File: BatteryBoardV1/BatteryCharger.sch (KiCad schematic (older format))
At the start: 11 parts, among them J1 Conn_01x04_Male, Q1 Q_NMOS_GSD, U1 MCP73213

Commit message: Rearrange components to add mounting holes and silkscreen
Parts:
- added MK1, MK2, MK3: Mounting_Hole, Mounting_Holes:MountingHole_3.2mm_M3, symbol Mounting_Hole
- J1: renamed from JIn1; footprint Connectors:Barrel_Jack_CUI_PJ-102AH -> SOAR_Kicad_Library:CUI_PJ-102A_2.5mm_DC_JACK
- J2: renamed from JIn2; footprint TerminalBlock_Phoenix:TerminalBlock_Phoenix_PT-1,5-2-5.0-H_1x02_P5.00mm_Horizontal -> SOAR_Kicad_Library:TerminalBlock_5mm_2POS_ED2600
- J3: renamed from J1; footprint SOAR_Library:Molex_Micro-Fit_3.0_43045-0400_2x02_P3.00mm_Horizontal -> SOAR_Kicad_Library:Molex_Micro-Fit_3.0_43045-0400_2x02_P3.00mm_Horizontal
- J4: renamed from JOut1; footprint TerminalBlock_Phoenix:TerminalBlock_Phoenix_PT-1,5-2-5.0-H_1x02_P5.00mm_Horizontal -> SOAR_Kicad_Library:TerminalBlock_5mm_2POS_ED2600
- renumbered C2 to C1, C1 to C2
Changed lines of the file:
@@
 LIBS:valves
 LIBS:BatCharge
-LIBS:Connectors
-LIBS:dk_Addressable-Specialty
-LIBS:dk_Alarms-Buzzers-and-Sirens
-LIBS:dk_Automotive-Relays
-LIBS:dk_Balun
-LIBS:dk_Barrel-Audio-Connectors
-LIBS:dk_Battery-Holders-Clips-Contacts
-LIBS:dk_Clock-Timing-Clock-Generators-PLLs-Frequency-Synthesizers
-LIBS:dk_Clock-Timing-Programmable-Timers-and-Oscillators
-LIBS:dk_Clock-Timing-Real-Time-Clocks
-LIBS:dk_Coaxial-Connectors-RF
-LIBS:dk_Current-Transducers
-LIBS:dk_Data-Acquisition-ADCs-DACs-Special-Purpose
-LIBS:dk_Data-Acquisition-Analog-to-Digital-Converters-ADC
-LIBS:dk_Data-Acquisition-Digital-Potentiometers
-LIBS:dk_Data-Acquisition-Digital-to-Analog-Converters-DAC
-LIBS:dk_Data-Acquisition-Touch-Screen-Controllers
-LIBS:dk_DC-DC-Converters
-LIBS:dk_Digital-Isolators
-LIBS:dk_Diodes-Bridge-Rectifiers
-LIBS:dk_Diodes-Rectifiers-Arrays
-LIBS:dk_Diodes-Rectifiers-Single
-LIBS:dk_Diodes-Zener-Single
-LIBS:dk_Display-Modules-LED-Character-and-Numeric
-LIBS:dk_D-Sub-Connectors
-LIBS:dk_Embedded-Microcontrollers
-LIBS:dk_Encoders
-LIBS:dk_Evaluation-Boards-Sensors
-LIBS:dk_Ferrite-Beads-and-Chips
-LIBS:dk_Fixed-Inductors
-LIBS:dk_Fuses
-LIBS:dk_Gas-Sensors
-LIBS:dk_Humidity-Moisture-Sensors
-LIBS:dk_Image-Sensors-Camera
-LIBS:dk_Infrared-UV-Visible-Emitters
-LIBS:dk_Inrush-Current-Limiters-ICL
-LIBS:dk_Interface-Analog-Switches-Multiplexers-Demultiplexers
-LIBS:dk_Interface-Analog-Switches-Special-Purpose
-LIBS:dk_Interface-Controllers
-LIBS:dk_Interface-Drivers-Receivers-Transceivers
-LIBS:dk_Interface-I-O-Expanders
-LIBS:dk_Interface-Modules
-LIBS:dk_Interface-Sensor-and-Detector-Interfaces
-LIBS:dk_Interface-Sensor-Capacitive-Touch
-LIBS:dk_Interface-Specialized
-LIBS:dk_LED-Indication-Discrete
-LIBS:dk_LEDs-Circuit-Board-Indicators-Arrays-Light-Bars-Bar-Graphs
-LIBS:dk_Linear-Amplifiers-Audio
-LIBS:dk_Linear-Amplifiers-Instrumentation-OP-Amps-Buffer-Amps
-LIBS:dk_Linear-Comparators
-LIBS:dk_Logic-Buffers-Drivers-Receivers-Transceivers
-LIBS:dk_Logic-Flip-Flops
-LIBS:dk_Logic-Gates-and-Inverters
-LIBS:dk_Logic-Multivibrators
-LIBS:dk_Logic-Shift-Registers
-LIBS:dk_Logic-Signal-Switches-Multiplexers-Decoders
-LIBS:dk_Logic-Translators-Level-Shifters
-LIBS:dk_Magnetic-Sensors-Compass-Magnetic-Field-Modules
-LIBS:dk_Magnetic-Sensors-Linear-Compass-ICs
-LIBS:dk_Magnetic-Sensors-Switches-Solid-State
-LIBS:dk_Memory
-LIBS:dk_Memory-Connectors-PC-Card-Sockets
-LIBS:dk_Microphones
-LIBS:dk_Modular-Connectors-Jacks
-LIBS:dk_Modular-Connectors-Jacks-With-Magnetics
-LIBS:dk_Motion-Sensors-Accelerometers
-LIBS:dk_Motion-Sensors-IMUs-Inertial-Measurement-Units
-LIBS:dk_Motion-Sensors-Tilt-Switches
-LIBS:dk_Navigation-Switches-Joystick
-LIBS:dk_Optical-Sensors-Ambient-Light-IR-UV-Sensors
-LIBS:dk_Optical-Sensors-Photo-Detectors-Remote-Receiver
-LIBS:dk_Optical-Sensors-Photodiodes
-LIBS:dk_Optical-Sensors-Phototransistors
-LIBS:dk_Optical-Sensors-Reflective-Analog-Output
-LIBS:dk_Optoisolators-Logic-Output
-LIBS:dk_Optoisolators-Transistor-Photovoltaic-Output
-LIBS:dk_Optoisolators-Triac-SCR-Output
-LIBS:dk_Oscillators
-LIBS:dk_PMIC-AC-DC-Converters-Offline-Switchers
-LIBS:dk_PMIC-Battery-Chargers
-LIBS:dk_PMIC-Battery-Management
-LIBS:dk_PMIC-Current-Regulation-Management
-LIBS:dk_PMIC-Full-Half-Bridge-Drivers
-LIBS:dk_PMIC-Gate-Drivers
-LIBS:dk_PMIC-LED-Drivers
-LIBS:dk_PMIC-Motor-Drivers-Controllers
-LIBS:dk_PMIC-OR-Controllers-Ideal-Diodes
-LIBS:dk_PMIC-Power-Distribution-Switches-Load-Drivers
-LIBS:dk_PMIC-Power-Management-Specialized
-LIBS:dk_PMIC-RMS-to-DC-Converters
-LIBS:dk_PMIC-Supervisors
-LIBS:dk_PMIC-Thermal-Management
-LIBS:dk_PMIC-V-F-and-F-V-Converters
-LIBS:dk_PMIC-Voltage-Reference
-LIBS:dk_PMIC-Voltage-Regulators-DC-DC-Switching-Controllers
-LIBS:dk_PMIC-Voltage-Regulators-DC-DC-Switching-Regulators
-LIBS:dk_PMIC-Voltage-Regulators-Linear
-LIBS:dk_PMIC-Voltage-Regulators-Special-Purpose
-LIBS:dk_Power-Relays-Over-2-Amps
-LIBS:dk_Pressure-Sensors-Transducers
-LIBS:dk_Programmable-Oscillators
-LIBS:dk_Pushbutton-Switches
-LIBS:dk_Rectangular-Connectors-Headers-Male-Pins
-LIBS:dk_Reed-Relays
-LIBS:dk_Resistor-Networks-Arrays
-LIBS:dk_RF-Amplifiers
-LIBS:dk_RF-Antennas
-LIBS:dk_RF-Demodulators
-LIBS:dk_RF-Detectors
-LIBS:dk_RF-Evaluation-and-Development-Kits-Boards
-LIBS:dk_RFID-RF-Access-Monitoring-ICs
-LIBS:dk_RF-Receivers
-LIBS:dk_RF-Switches
-LIBS:dk_RF-Transceiver-ICs
-LIBS:dk_RF-Transceiver-Modules
-LIBS:dk_RF-Transmitters
-LIBS:dk_Rotary-Potentiometers-Rheostats
-LIBS:dk_Sensors-Transducers_Accessories
-LIBS:dk_Signal-Relays-Up-to-2-Amps
-LIBS:dk_Slide-Switches
-LIBS:dk_Solid-State-Relays
-LIBS:dk_Specialized-ICs
-LIBS:dk_Specialized-Sensors
-LIBS:dk_Surge-Suppression-ICs
-LIBS:dk_Tactile-Switches
-LIBS:dk_Temperature-Sensors-Analog-and-Digital-Output
-LIBS:dk_Thermal-Cutoffs-Thermal-Fuses
-LIBS:dk_Thyristors-DIACs-SIDACs
-LIBS:dk_Thyristors-SCRs
-LIBS:dk_Thyristors-TRIACs
-LIBS:dk_Toggle-Switches
-LIBS:dk_Transistors-Bipolar-BJT-Arrays
-LIBS:dk_Transistors-Bipolar-BJT-RF
-LIBS:dk_Transistors-Bipolar-BJT-Single
-LIBS:dk_Transistors-Bipolar-BJT-Single-Pre-Biased
-LIBS:dk_Transistors-FETs-MOSFETs-Arrays
-LIBS:dk_Transistors-FETs-MOSFETs-RF
-LIBS:dk_Transistors-FETs-MOSFETs-Single
-LIBS:dk_Transistors-JFETs
-LIBS:dk_Trimmer-Potentiometers
-LIBS:dk_TVS-Diodes
-LIBS:dk_TVS-Mixed-Technology
-LIBS:dk_USB-DVI-HDMI-Connectors
+LIBS:mechanical
 LIBS:BatteryCharger-cache
 EELAYER 25 0
@@
 $EndComp
 $Comp
-L C C2
+L C C1
 U 1 1 5A5FF651
 P 4225 4225
-F 0 "C2" H 4250 4325 50  0000 L CNN
+F 0 "C1" H 4250 4325 50  0000 L CNN
 F 1 "4.7u" H 4250 4125 50  0000 L CNN
 F 2 "Capacitors_SMD:C_0805_HandSoldering" H 4263 4075 50  0001 C CNN
@@
 $EndComp
 $Comp
-L C C1
+L C C2
 U 1 1 5A5FF66F
 P 5100 4550
-F 0 "C1" H 5125 4650 50  0000 L CNN
+F 0 "C2" H 5125 4650 50  0000 L CNN
 F 1 "4.7u" H 5125 4450 50  0000 L CNN
 F 2 "Capacitors_SMD:C_0805_HandSoldering" H 5138 4400 50  0001 C CNN
@@
 $EndComp
 $Comp
-L Screw_Terminal_01x02 JOut1
+L Screw_Terminal_01x02 J4
 U 1 1 5A8B62D4
 P 5875 5400
-F 0 "JOut1" V 5875 5575 50  0000 C CNN
+F 0 "J4" V 5875 5575 50  0000 C CNN
 F 1 "Bat.Terms." V 5975 5350 50  0000 C CNN
-F 2 "TerminalBlock_Phoenix:TerminalBlock_Phoenix_PT-1,5-2-5.0-H_1x02_P5.00mm_Horizontal" H 5875 5400 50  0001 C CNN
+F 2 "SOAR_Kicad_Library:TerminalBlock_5mm_2POS_ED2600" H 5875 5400 50  0001 C CNN
 F 3 "" H 5875 5400 50  0001 C CNN
 	1    5875 5400
@@
 $EndComp
 $Comp
-L Barrel_Jack JIn1
+L Barrel_Jack J1
 U 1 1 5A8B83C9
 P 1600 3850
-F 0 "JIn1" H 1600 4060 50  0000 C CNN
+F 0 "J1" H 1600 4060 50  0000 C CNN
 F 1 "Barrel_Jack" H 1600 3675 50  0000 C CNN
-F 2 "Connectors:Barrel_Jack_CUI_PJ-102AH" H 1650 3810 50  0001 C CNN
+F 2 "SOAR_Kicad_Library:CUI_PJ-102A_2.5mm_DC_JACK" H 1650 3810 50  0001 C CNN
 F 3 "" H 1650 3810 50  0001 C CNN
 	1    1600 3850
@@
 $EndComp
 $Comp
-L Screw_Terminal_01x02 JIn2
+L Screw_Terminal_01x02 J2
 U 1 1 5A8B7334
 P 2150 4975
-F 0 "JIn2" H 2150 5075 50  0000 C CNN
+F 0 "J2" H 2150 5075 50  0000 C CNN
 F 1 "Input Terms." V 2250 4925 50  0000 C CNN
-F 2 "TerminalBlock_Phoenix:TerminalBlock_Phoenix_PT-1,5-2-5.0-H_1x02_P5.00mm_Horizontal" H 2150 4975 50  0001 C CNN
+F 2 "SOAR_Kicad_Library:TerminalBlock_5mm_2POS_ED2600" H 2150 4975 50  0001 C CNN
 F 3 "" H 2150 4975 50  0001 C CNN
 	1    2150 4975
@@
 	4800 1975 5975 1975
 $Comp
-L Conn_01x04_Male J1
+L Conn_01x04_Male J3
 U 1 1 5AC40877
 P 5225 6625
-F 0 "J1" H 5225 6825 50  0000 C CNN
+F 0 "J3" H 5225 6825 50  0000 C CNN
 F 1 "Conn_01x04_Male" H 5225 6325 50  0000 C CNN
-F 2 "SOAR_Library:Molex_Micro-Fit_3.0_43045-0400_2x02_P3.00mm_Horizontal" H 5225 6625 50  0001 C CNN
+F 2 "SOAR_Kicad_Library:Molex_Micro-Fit_3.0_43045-0400_2x02_P3.00mm_Horizontal" H 5225 6625 50  0001 C CNN
 F 3 "" H 5225 6625 50  0001 C CNN
 	1    5225 6625
@@
 	5200 6200 5200 5600
 Connection ~ 5200 5600
+$Comp
+L Mounting_Hole MK1
+U 1 1 5AEDFDB9
+P 1030 7175
+F 0 "MK1" H 1030 7375 50  0000 C CNN
+F 1 "Mounting_Hole" H 1030 7300 50  0000 C CNN
+F 2 "Mounting_Holes:MountingHole_3.2mm_M3" H 1030 7175 50  0001 C CNN
+F 3 "" H 1030 7175 50  0001 C CNN
+	1    1030 7175
+	1    0    0    -1
+$EndComp
+$Comp
+L Mounting_Hole MK2
+U 1 1 5AEE0072
+P 1670 7170
+F 0 "MK2" H 1670 7370 50  0000 C CNN
+F 1 "Mounting_Hole" H 1670 7295 50  0000 C CNN
+F 2 "Mounting_Holes:MountingHole_3.2mm_M3" H 1670 7170 50  0001 C CNN
+F 3 "" H 1670 7170 50  0001 C CNN
+	1    1670 7170
+	1    0    0    -1
+$EndComp
+$Comp
+L Mounting_Hole MK3
+U 1 1 5AEE06B8
+P 2300 7175
+F 0 "MK3" H 2300 7375 50  0000 C CNN
+F 1 "Mounting_Hole" H 2300 7300 50  0000 C CNN
+F 2 "Mounting_Holes:MountingHole_3.2mm_M3" H 2300 7175 50  0001 C CNN
+F 3 "" H 2300 7175 50  0001 C CNN
+	1    2300 7175
+	1    0    0    -1
+$EndComp
 $EndSCHEMATC

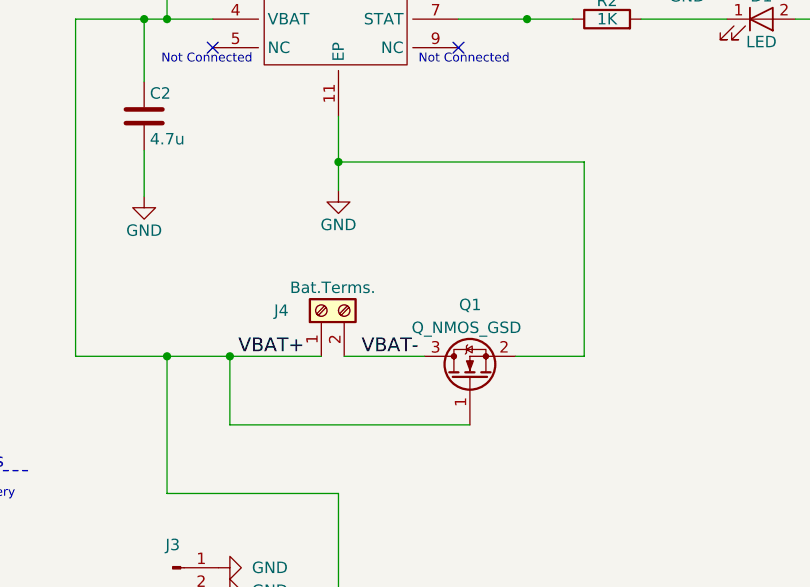
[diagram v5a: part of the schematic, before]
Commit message: final design published. Gerbers and schematic PDF generated.
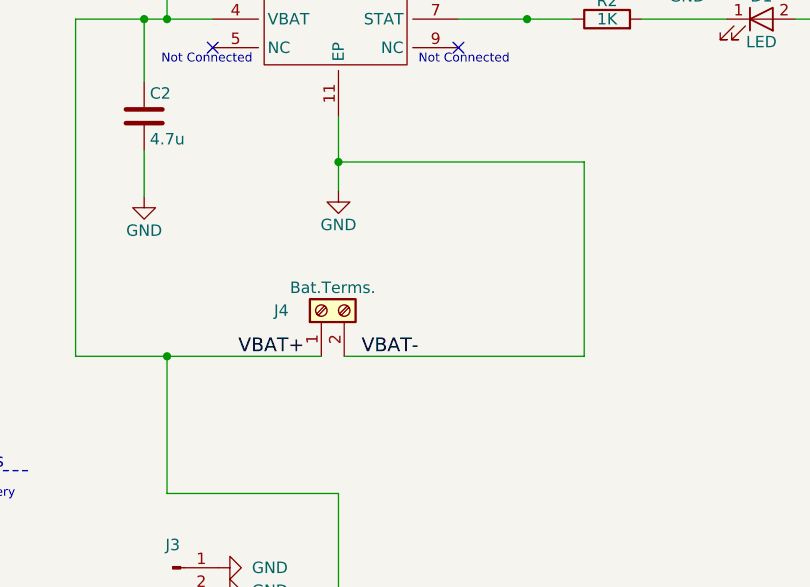
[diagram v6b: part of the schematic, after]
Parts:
- removed Q1: Q_NMOS_GSD, TO_SOT_Packages_SMD:SOT-23, symbol Q_NMOS_GSD
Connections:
- net VBAT- is gone; now on net GND: J4.2 (Pin_2)
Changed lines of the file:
@@
 	0    1    1    0
-$EndComp
-$Comp
-L Q_NMOS_GSD Q1
-U 1 1 5A9AF155
-P 6525 5700
-F 0 "Q1" V 6850 5650 50  0000 L CNN
-F 1 "Q_NMOS_GSD" V 6750 5475 50  0000 L CNN
-F 2 "TO_SOT_Packages_SMD:SOT-23" H 6725 5800 50  0001 C CNN
-F 3 "" H 6525 5700 50  0001 C CNN
-	1    6525 5700
-	0    -1   -1   0
 $EndComp
 NoConn ~ 6475 4250
@@
 Connection ~ 6775 4125
 Wire Wire Line
-	6325 5600 5975 5600
+	5975 5600 7025 5600
 Wire Wire Line
 	4800 4125 4800 5600
@@
 	2325 4775 2150 4775
 Wire Wire Line
-	7025 4750 7025 5600
-Wire Wire Line
-	7025 5600 6725 5600
-Wire Wire Line
-	6525 5900 5475 5900
-Wire Wire Line
-	5475 5900 5475 5600
-Connection ~ 5475 5600
+	7025 5600 7025 4750
 Wire Notes Line
 	1425 3000 2425 3000
